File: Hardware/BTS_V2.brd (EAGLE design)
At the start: 113 x 79.4 mm, 68 parts, among them IC1 TPA3140D2PWP, IC2 BLK-MD-SPK-B, J1 SPKR_OUT, J2 RN52BoB_R, J3 RN52BoB_L, J4 TFT_CONNECTION, J6 HC-05, T3_2 TEENSY_3.1-3.2_DIL

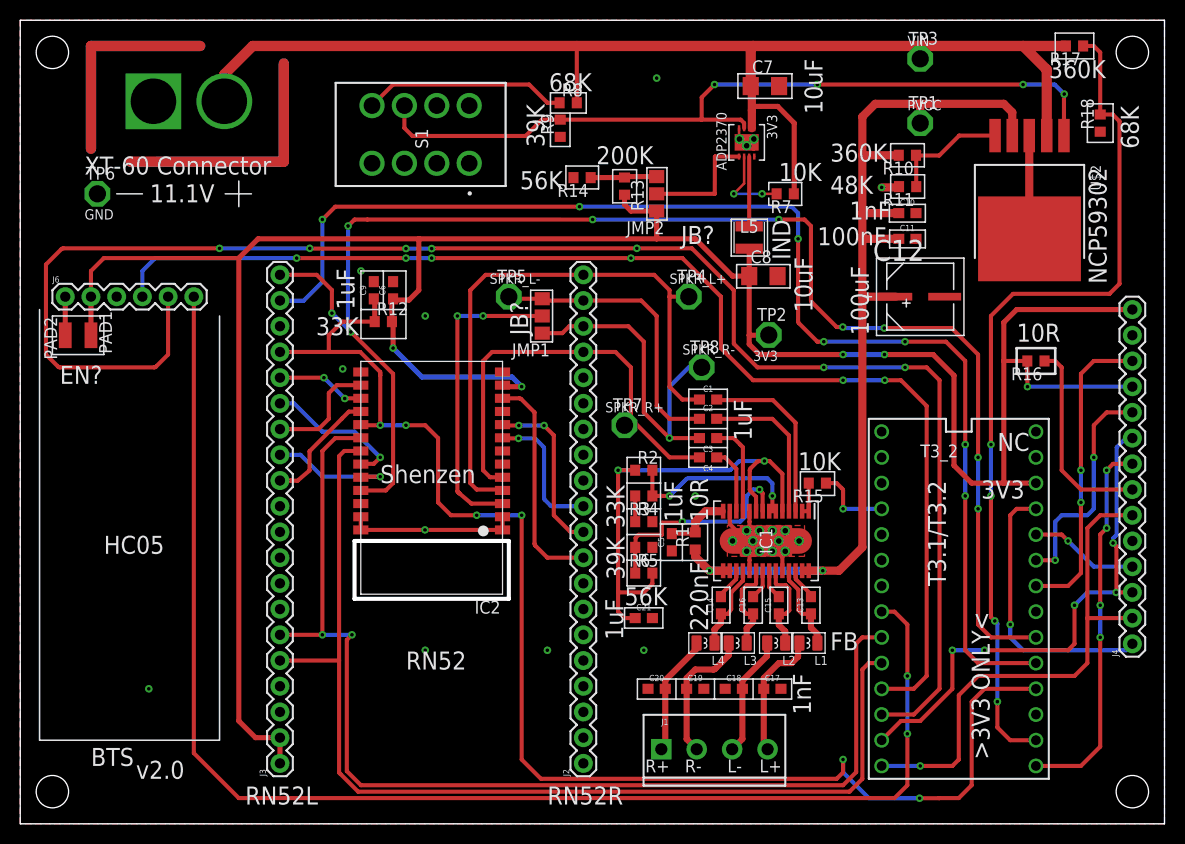
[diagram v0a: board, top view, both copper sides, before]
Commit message: Fixed two HW issues
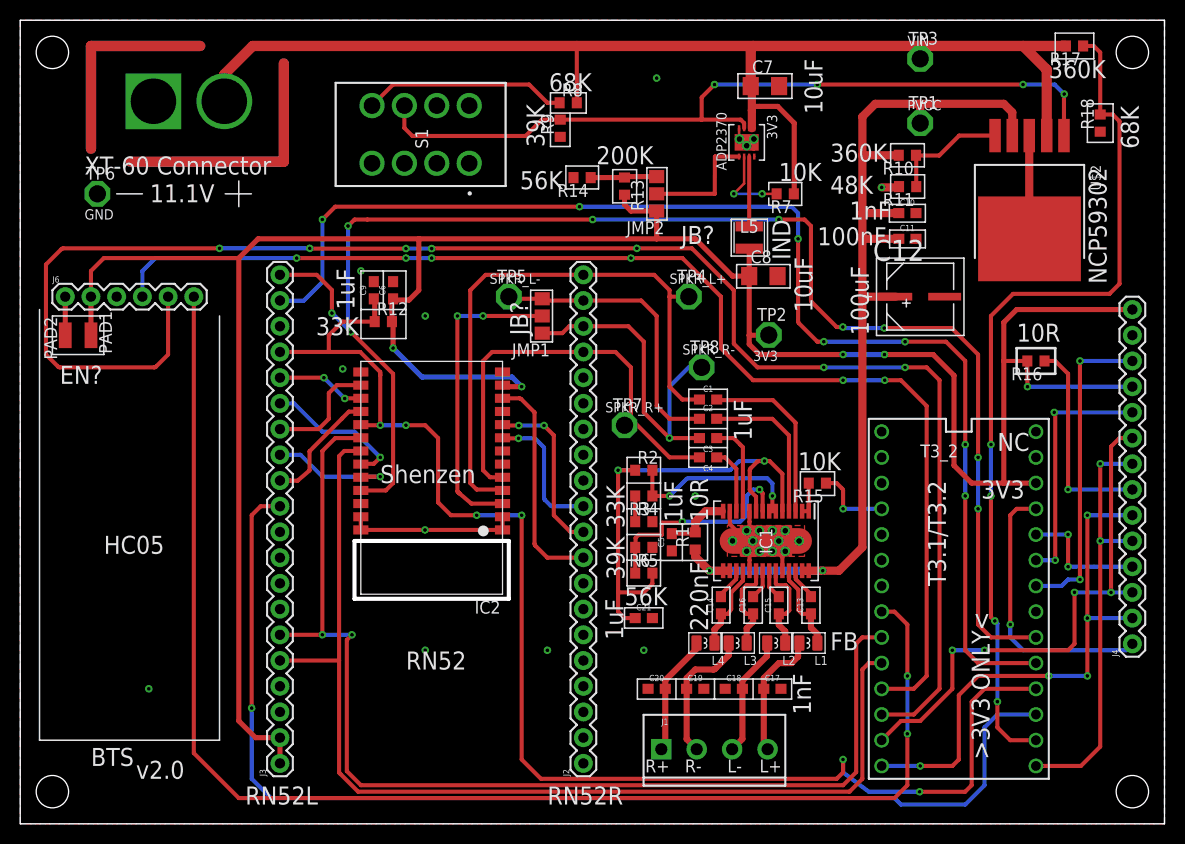
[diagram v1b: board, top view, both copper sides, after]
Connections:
- removed net D15: T3_2.15/A1
- removed net TCLK: J4.5
- net DSCK: now also J4.5
- net GPIO9: now also T3_2.15/A1
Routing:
- net GPIO9: track 0.00 -> 114.7 mm, vias 0 -> 1
- net DSCK: track 38.8 -> 41.4 mm, vias 4 -> 2
- net D/C: track 22.6 -> 24.9 mm
- net TCS: track 10.8 -> 12.7 mm, vias 1 -> 2
- net DMISO: track 51.0 -> 52.5 mm, vias 1 -> 5
- net DCS: track 30.3 -> 31.4 mm
- net DMOSI: track 51.8 -> 52.9 mm, vias 5 -> 4
- net LED: track 19.9 -> 20.6 mm, vias 0 -> 1
- net GPIO4: track 137.5 -> 136.8 mm
